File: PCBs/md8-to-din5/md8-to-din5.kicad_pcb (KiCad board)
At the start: 2 copper layers, 14.2 x 36.9 mm, 4 parts, among them J1 DIN-5_180degree_female, J2 Mini-DIN-8_male, J3 RX/TX straight/null, J4 DTR/DSR straight/null

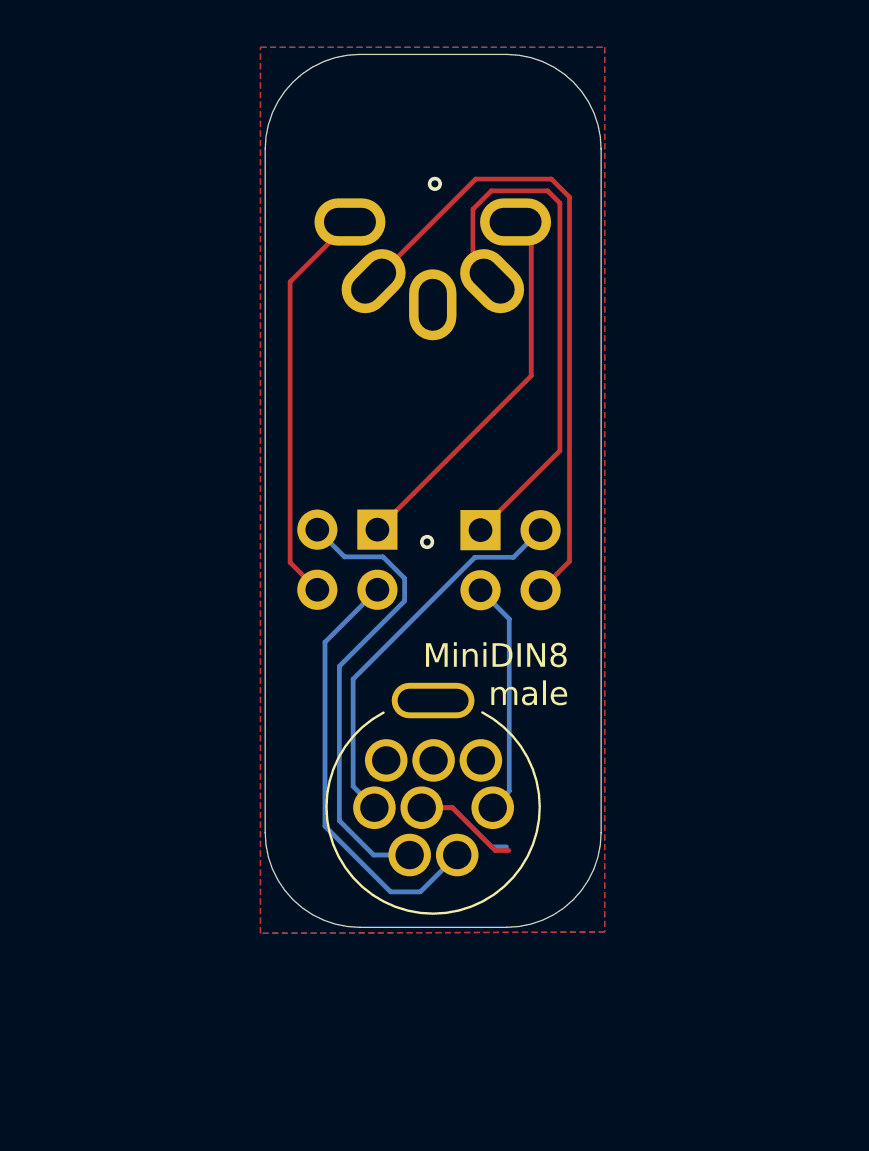
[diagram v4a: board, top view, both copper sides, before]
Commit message: Add gpio-fan ability
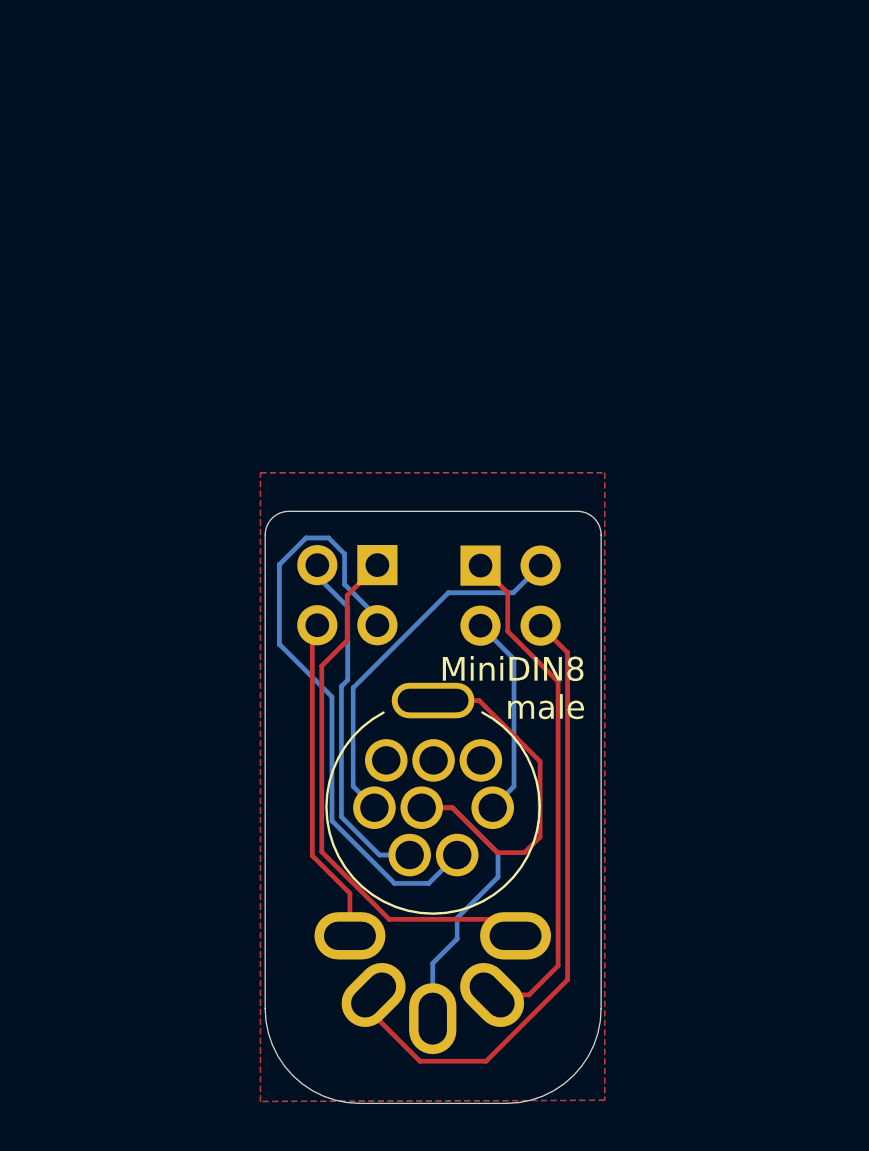
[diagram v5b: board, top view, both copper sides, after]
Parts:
- moved J1 30.2 mm to (184.0, 117.7)
- moved J4 1.50 mm to (181.6, 98.5)
- moved J3 1.50 mm to (186.0, 98.5)
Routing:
- net GND: track 8.70 -> 27.0 mm, vias 2 -> 0
- net Net-(J4-Pin_3): track 18.3 -> 25.7 mm
- net Net-(J4-Pin_1): track 16.0 -> 22.8 mm
- net Net-(J4-Pin_2): track 19.5 -> 14.8 mm
- net Net-(J4-Pin_4): track 17.1 -> 13.9 mm
- net Net-(J3-Pin_2): track 9.99 -> 8.65 mm
- net Net-(J3-Pin_1): track 22.8 -> 21.6 mm
- net Net-(J3-Pin_3): track 16.3 -> 15.5 mm
- net Net-(J3-Pin_4): track 27.5 -> 26.7 mm
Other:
- board size 14.2 x 36.9 mm -> 14.2 x 25 mm
- board text added: "↔ NM ↕ ST"
- board text removed: "↔ straight ↕ cross"
